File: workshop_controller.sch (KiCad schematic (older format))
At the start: 20 parts, among them J1 Conn_02x10_Odd_Even, J2 Conn_02x10_Odd_Even, J3 AudioJack3, J4 Micro_SD_Card_Det, J5 Conn_02x25_Odd_Even, SW1 SW_Push, SW2 SW_Push, U1 MPU-9250, U2 BME280, U3 MCP23S17_SS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

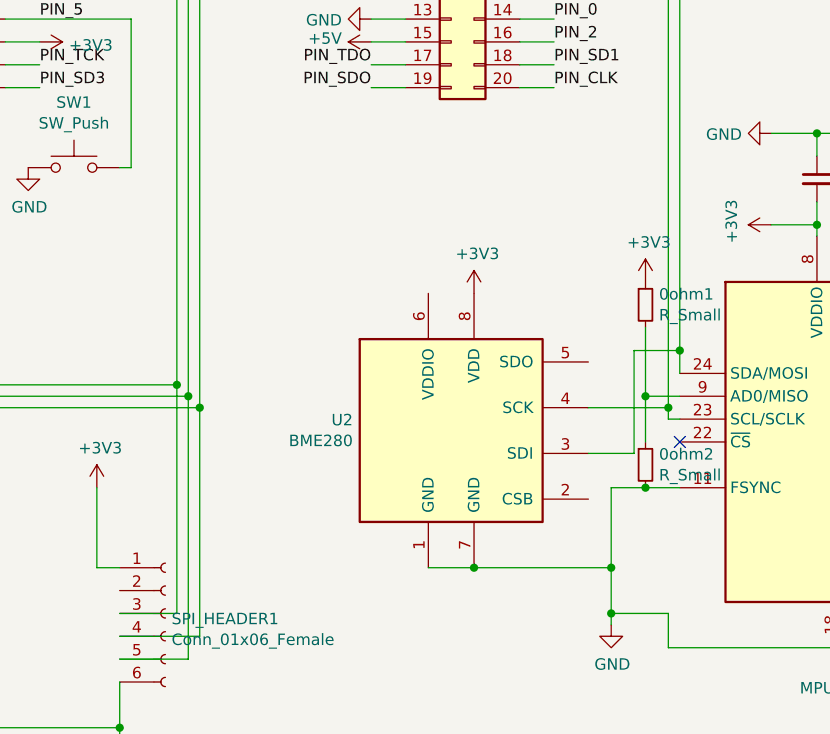
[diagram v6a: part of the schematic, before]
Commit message: connect bme280
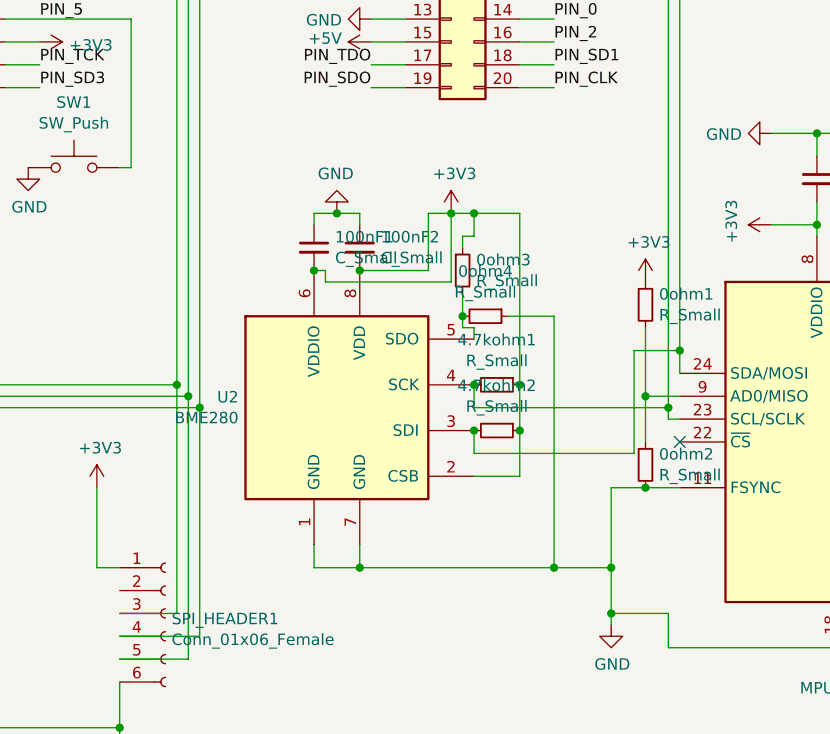
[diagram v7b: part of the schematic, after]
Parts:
- added 0ohm3, 0ohm4, 4.7kohm1, 4.7kohm2: R_Small, symbol Device:R_Small
- added 100nF1, 100nF2: C_Small, symbol Device:C_Small
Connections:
- net +3V3: now also U2.2 (CSB), U2.6 (VDDIO), 0ohm3.1, 100nF1.2, 100nF2.2, 4.7kohm1.1, 4.7kohm2.1
- net GND: now also 0ohm4.1, 100nF1.1, 100nF2.1
- net PIN_25: now also 4.7kohm2.2
- net PIN_27: now also 4.7kohm1.2
- net at U2.5 (SDO): now also 0ohm3.2, 0ohm4.2
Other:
- moved on the sheet: U2
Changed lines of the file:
@@
-$EndComp
-$Comp
-L Sensor:BME280 U2
-U 1 1 5CA64E9A
-P 7000 5300
-F 0 "U2" H 6570 5346 50  0000 R CNN
-F 1 "BME280" H 6570 5255 50  0000 R CNN
-F 2 "Package_LGA:Bosch_LGA-8_2.5x2.5mm_P0.65mm_ClockwisePinNumbering" H 7000 5100 50  0001 C CNN
-F 3 "https://ae-bst.resource.bosch.com/media/_tech/media/datasheets/BST-BME280_DS001-11.pdf" H 7000 5100 50  0001 C CNN
-	1    7000 5300
-	1    0    0    -1
 $EndComp
 $Comp
@@
 L power:+3V3 #PWR0111
 U 1 1 5CA917C5
-P 7100 4700
-F 0 "#PWR0111" H 7100 4550 50  0001 C CNN
-F 1 "+3V3" H 7115 4873 50  0000 C CNN
-F 2 "" H 7100 4700 50  0001 C CNN
-F 3 "" H 7100 4700 50  0001 C CNN
-	1    7100 4700
-	1    0    0    -1
-$EndComp
-Wire Wire Line
-	7600 5200 7950 5200
+P 7000 4350
+F 0 "#PWR0111" H 7000 4200 50  0001 C CNN
+F 1 "+3V3" H 7015 4523 50  0000 C CNN
+F 2 "" H 7000 4350 50  0001 C CNN
+F 3 "" H 7000 4350 50  0001 C CNN
+	1    7000 4350
+	1    0    0    -1
+$EndComp
 Connection ~ 7950 5200
 Wire Wire Line
 	7950 5200 7950 5250
-Wire Wire Line
-	7600 5400 7800 5400
 Wire Wire Line
 	7800 5400 7800 4950
@@
 $EndComp
 Wire Wire Line
-	7100 5900 7700 5900
-Wire Wire Line
 	7700 5900 7700 6100
-Wire Wire Line
-	6900 5900 7100 5900
-Connection ~ 7100 5900
 Wire Wire Line
 	8700 6250 7950 6250
@@
 	7850 5350 7850 5150
 Connection ~ 7850 5150
+Wire Wire Line
+	6400 5800 6400 5900
+Wire Wire Line
+	6400 5900 6600 5900
+Wire Wire Line
+	6600 5800 6600 5900
+Connection ~ 6600 5900
+Wire Wire Line
+	6600 5900 7450 5900
+Wire Wire Line
+	7100 5500 7300 5500
+$Comp
+L Device:C_Small 100nF1
+U 1 1 5CB26720
+P 6400 4500
+F 0 "100nF1" H 6492 4546 50  0000 L CNN
+F 1 "C_Small" H 6492 4455 50  0000 L CNN
+F 2 "" H 6400 4500 50  0001 C CNN
+F 3 "~" H 6400 4500 50  0001 C CNN
+	1    6400 4500
+	1    0    0    -1
+$EndComp
+Wire Wire Line
+	6600 4600 6900 4600
+$Comp
+L Device:C_Small 100nF2
+U 1 1 5CB2F53A
+P 6600 4500
+F 0 "100nF2" H 6692 4546 50  0000 L CNN
+F 1 "C_Small" H 6692 4455 50  0000 L CNN
+F 2 "" H 6600 4500 50  0001 C CNN
+F 3 "~" H 6600 4500 50  0001 C CNN
+	1    6600 4500
+	1    0    0    -1
+$EndComp
+$Comp
+L power:GND #PWR?
+U 1 1 5CB33AA1
+P 6500 4350
+F 0 "#PWR?" H 6500 4100 50  0001 C CNN
+F 1 "GND" H 6505 4177 50  0000 C CNN
+F 2 "" H 6500 4350 50  0001 C CNN
+F 3 "" H 6500 4350 50  0001 C CNN
+	1    6500 4350
+	-1   0    0    1
+$EndComp
+Wire Wire Line
+	7000 4650 7000 4350
+Wire Wire Line
+	7000 4350 6900 4350
+Wire Wire Line
+	6900 4350 6900 4600
+Connection ~ 7000 4350
+Wire Wire Line
+	7300 4350 7300 5100
+$Comp
+L Device:R_Small 4.7kohm2
+U 1 1 5CB4F8F9
+P 7200 5300
+F 0 "4.7kohm2" V 7004 5300 50  0000 C CNN
+F 1 "R_Small" V 7095 5300 50  0000 C CNN
+F 2 "" H 7200 5300 50  0001 C CNN
+F 3 "~" H 7200 5300 50  0001 C CNN
+	1    7200 5300
+	0    1    1    0
+$EndComp
+Connection ~ 7300 5300
+Wire Wire Line
+	7300 5300 7300 5500
+$Comp
+L Device:R_Small 4.7kohm1
+U 1 1 5CB4F9EF
+P 7200 5100
+F 0 "4.7kohm1" V 7004 5100 50  0000 C CNN
+F 1 "R_Small" V 7095 5100 50  0000 C CNN
+F 2 "" H 7200 5100 50  0001 C CNN
+F 3 "~" H 7200 5100 50  0001 C CNN
+	1    7200 5100
+	0    1    1    0
+$EndComp
+Connection ~ 7300 5100
+Wire Wire Line
+	7300 5100 7300 5300
+Wire Wire Line
+	7100 5300 7100 5400
+Wire Wire Line
+	7100 5100 7100 5200
+$Comp
+L Device:R_Small 0ohm3
+U 1 1 5CB6002C
+P 7050 4600
+F 0 "0ohm3" H 7109 4646 50  0000 L CNN
+F 1 "R_Small" H 7109 4555 50  0000 L CNN
+F 2 "" H 7050 4600 50  0001 C CNN
+F 3 "~" H 7050 4600 50  0001 C CNN
+	1    7050 4600
+	1    0    0    -1
+$EndComp
+Connection ~ 6600 4600
+Connection ~ 7100 5100
+Connection ~ 7100 5300
+$Comp
+L Sensor:BME280 U2
+U 1 1 5CA64E9A
+P 6500 5200
+F 0 "U2" H 6070 5246 50  0000 R CNN
+F 1 "BME280" H 6070 5155 50  0000 R CNN
+F 2 "Package_LGA:Bosch_LGA-8_2.5x2.5mm_P0.65mm_ClockwisePinNumbering" H 6500 5000 50  0001 C CNN
+F 3 "https://ae-bst.resource.bosch.com/media/_tech/media/datasheets/BST-BME280_DS001-11.pdf" H 6500 5000 50  0001 C CNN
+	1    6500 5200
+	1    0    0    -1
+$EndComp
+Wire Wire Line
+	7100 4900 7100 4850
+Wire Wire Line
+	7100 4850 7050 4850
+Wire Wire Line
+	7050 4850 7050 4800
+$Comp
+L Device:R_Small 0ohm4
+U 1 1 5CB80FEA
+P 7150 4800
+F 0 "0ohm4" V 6954 4800 50  0000 C CNN
+F 1 "R_Small" V 7045 4800 50  0000 C CNN
+F 2 "" H 7150 4800 50  0001 C CNN
+F 3 "~" H 7150 4800 50  0001 C CNN
+	1    7150 4800
+	0    1    1    0
+$EndComp
+Connection ~ 7050 4800
+Wire Wire Line
+	7050 4800 7050 4700
+Wire Wire Line
+	7250 4800 7450 4800
+Wire Wire Line
+	7450 4800 7450 5900
+Connection ~ 7450 5900
+Wire Wire Line
+	7450 5900 7700 5900
+Wire Wire Line
+	7100 5200 7950 5200
+Wire Wire Line
+	7100 5400 7800 5400
+Wire Wire Line
+	6450 4650 6450 4600
+Wire Wire Line
+	6450 4600 6400 4600
+Wire Wire Line
+	6450 4650 7000 4650
+Connection ~ 6400 4600
+Wire Wire Line
+	6500 4350 6400 4350
+Wire Wire Line
+	6400 4350 6400 4400
+Wire Wire Line
+	6500 4350 6600 4350
+Wire Wire Line
+	6600 4350 6600 4400
+Connection ~ 6500 4350
+Wire Wire Line
+	7000 4350 7100 4350
+Wire Wire Line
+	7050 4500 7050 4450
+Wire Wire Line
+	7050 4450 7100 4450
+Wire Wire Line
+	7100 4450 7100 4350
+Connection ~ 7100 4350
+Wire Wire Line
+	7100 4350 7300 4350
 $EndSCHEMATC

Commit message: Add labels
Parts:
- removed J4: Micro_SD_Card_Det, symbol Connector:Micro_SD_Card_Det
- added J4: Micro_SD_Card, Connector_Card:microSD_HC_Wuerth_693072010801, symbol Connector:Micro_SD_Card
- added R3, R4, R5, R6, R7: 50kOhm, Resistor_SMD:R_1206_3216Metric_Pad1.42x1.75mm_HandSolder, symbol Device:R_Small
- added SW3, SW4: SW_Push, Button_Switch_THT:SW_PUSH-12mm_Wuerth-430476085716, symbol Switch:SW_Push
- 0ohm3, 0ohm4: footprint (none) -> Resistor_SMD:R_0603_1608Metric_Pad1.05x0.95mm_HandSolder
- C1: renamed from 100nF1; value C_Small -> 100nF; footprint (none) -> Capacitor_SMD:C_0603_1608Metric_Pad1.05x0.95mm_HandSolder
- C2: renamed from 100nF2; value C_Small -> 100nF; footprint (none) -> Capacitor_SMD:C_0603_1608Metric_Pad1.05x0.95mm_HandSolder
- C3: renamed from 0.1uF2; value C_Small -> 0.1µF
- C4: renamed from 10nF1; value C_Small -> 10nF
- C5: renamed from 0.1uF1; value C_Small -> 0.1µF
- R1: renamed from 4.7kohm1; value R_Small -> 4.7kohm; footprint (none) -> Resistor_SMD:R_0603_1608Metric_Pad1.05x0.95mm_HandSolder
- R2: renamed from 4.7kohm2; value R_Small -> 4.7kohm; footprint (none) -> Resistor_SMD:R_0603_1608Metric_Pad1.05x0.95mm_HandSolder
- SW1, SW2: footprint (none) -> Button_Switch_THT:SW_PUSH-12mm_Wuerth-430476085716
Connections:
- net labels added: DAC25, DAC26, I2C_SCK, I2C_SDA, JOY_X, JOY_Y, SS_HEADER1, SS_SDCARD, SS_TFT, SW1_PIN, SW2_PIN, SW3_PIN, SW4_PIN
- net labels removed: PIN_CS
- wire segments 146 -> 90
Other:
- moved on the sheet: 0ohm1, 0ohm2, 0ohm3, 0ohm4, C3, C4, C5, J3, JOYSTICK_LEFT1, LS1, MK1, R1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
